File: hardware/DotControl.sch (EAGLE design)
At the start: 36 parts, among them CN1 1X4-BIG, J3 USB-MICROB, SW2 Previous, SW5 Previous, SW6 Next, SW8 Ok, U1 ATMEGA328P-MU-QFN32, U2 TMP102, U3 ATSHA204-TSU, U4 SI7021

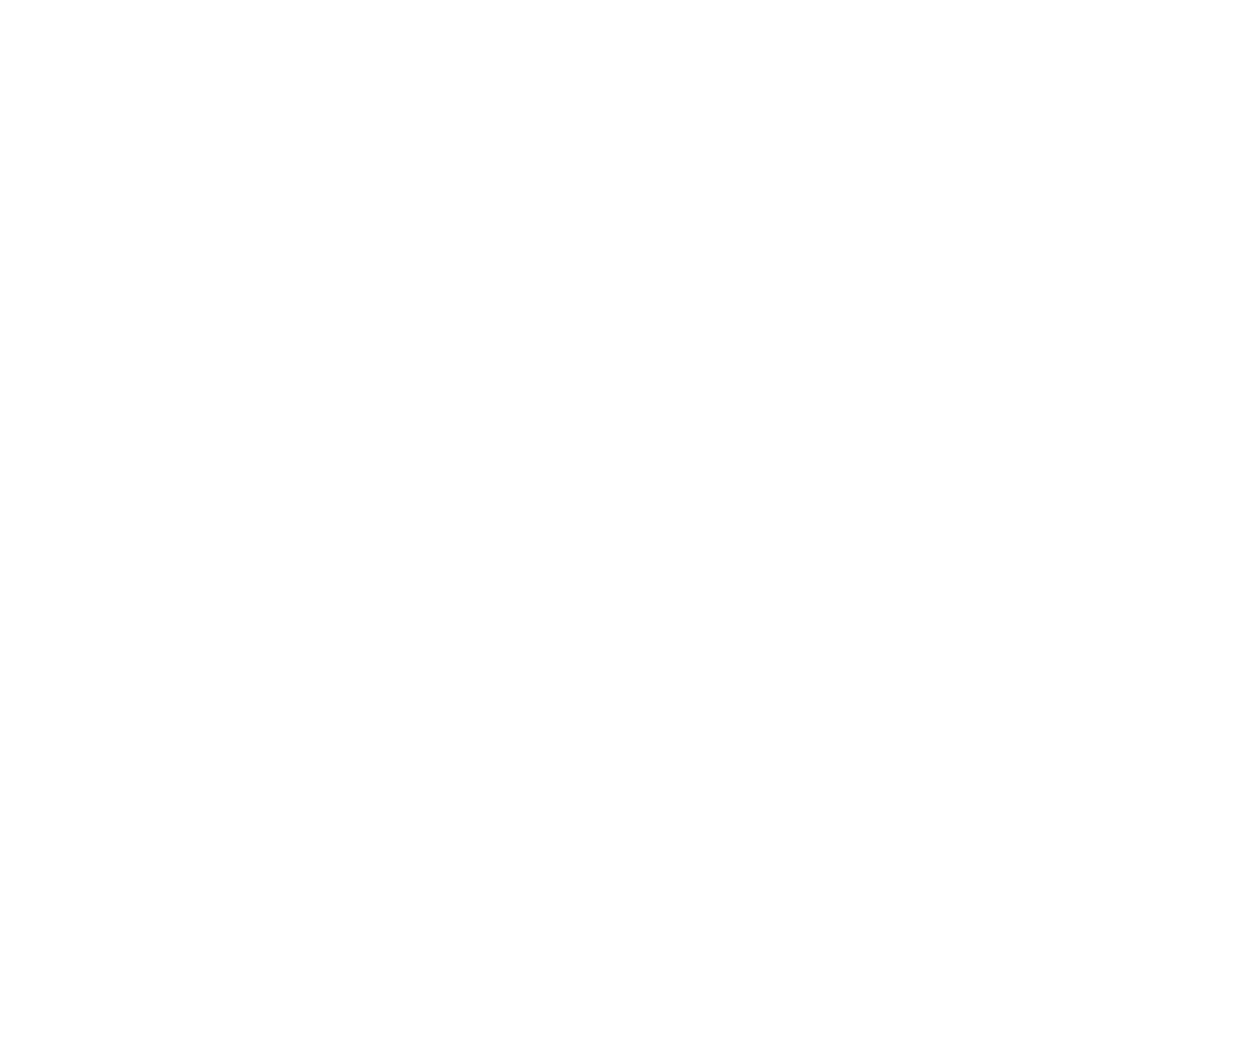
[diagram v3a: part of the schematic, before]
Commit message: [Beta] Add HW support for MPU9250
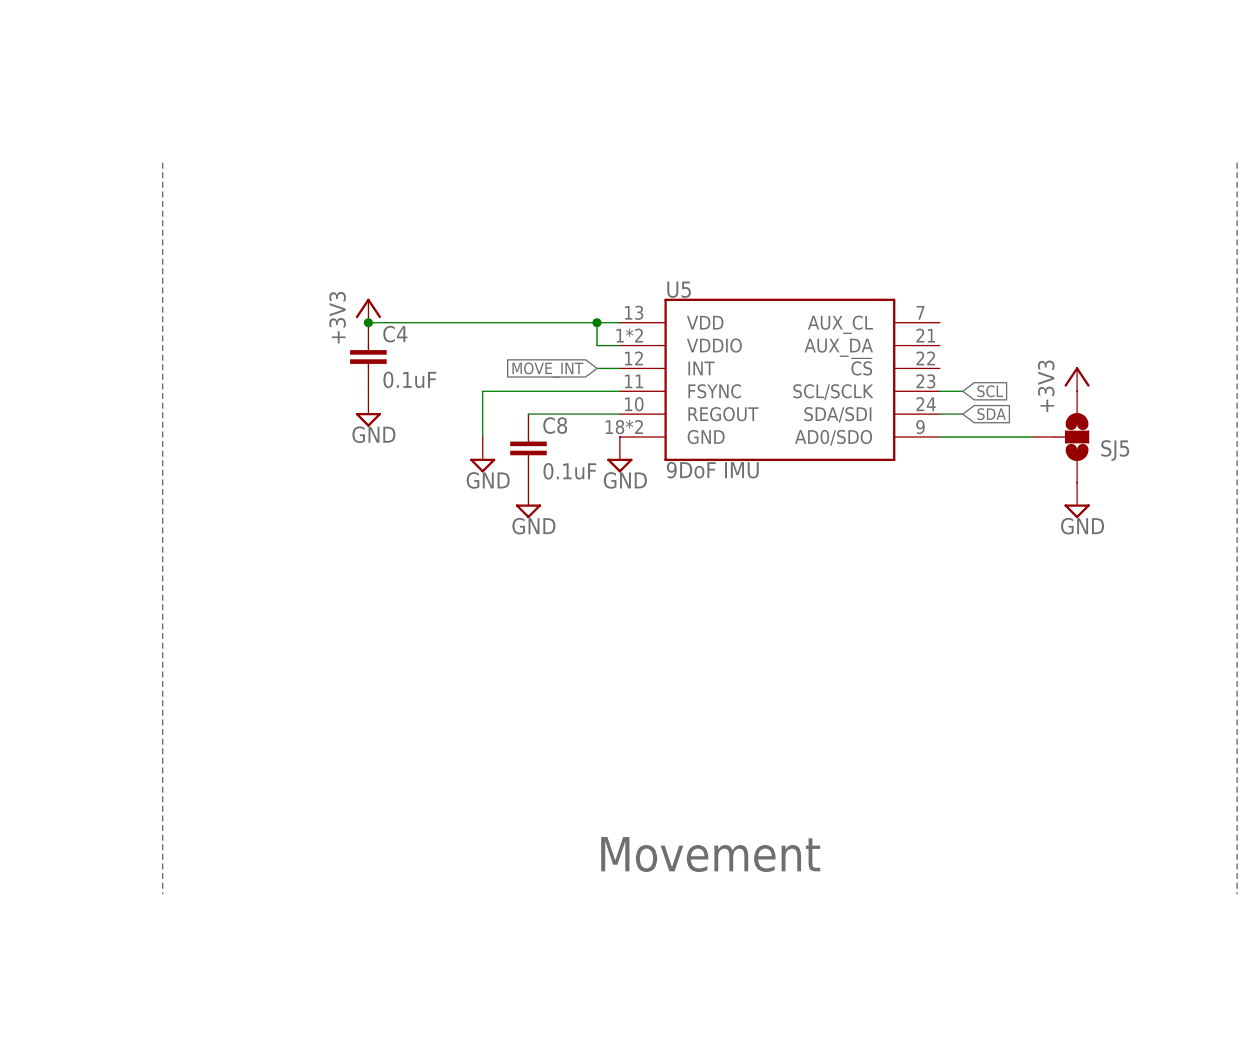
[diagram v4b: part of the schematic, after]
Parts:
- added C4, C8: 0.1uF, resistor:C-EUC0603
- added SJ5: (no value), SparkFun:SOLDERJUMPER_2WAYS
- added U5: 9DoF IMU, SparkFun-Sensors:MPU-9250
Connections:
- new net MOVE_INT: U5.INT
- new net N$10: SJ5.2, U5.AD0/SDO
- new net N$15: C8.1, U5.REGOUT
- net +3V3: now also C4.1, SJ5.3, U5.VDD, U5.VDDIO
- net GND: now also C4.2, C8.2, SJ5.1, U5.FSYNC, U5.GND
- net SCL: now also U5.SCL/SCLK
- net SDA: now also U5.SDA/SDI
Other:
- note added: "Movement"
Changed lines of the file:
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@@
 <setting verticaltext="up"/>
 </settings>
-<grid distance="0.05" unitdist="inch" unit="inch" style="lines" multiple="1" display="no" altdistance="0.01" altunitdist="inch" altunit="inch"/>
+<grid distance="0.1" unitdist="inch" unit="inch" style="lines" multiple="1" display="no" altdistance="0.01" altunitdist="inch" altunit="inch"/>
 <layers>
 <layer number="1" name="Top" color="4" fill="1" visible="no" active="no"/>
@@
 <part name="C10" library="adafruit" deviceset="CPOL-US" device="CT7343" value="1500uF 4V"/>
 <part name="SUPPLY16" library="supply2" deviceset="GND" device=""/>
+<part name="U5" library="SparkFun-Sensors" deviceset="MPU-9250" device="" value="9DoF IMU"/>
+<part name="SUPPLY23" library="supply2" deviceset="GND" device=""/>
+<part name="SJ5" library="SparkFun" deviceset="SOLDERJUMPER_2WAY" device="S"/>
+<part name="SUPPLY24" library="supply2" deviceset="GND" device=""/>
+<part name="+3V16" library="supply1" deviceset="+3V3" device=""/>
+<part name="C8" library="resistor" deviceset="C-EU" device="C0603" value="0.1uF"/>
+<part name="SUPPLY25" library="supply2" deviceset="GND" device=""/>
+<part name="+3V13" library="supply1" deviceset="+3V3" device=""/>
+<part name="C4" library="resistor" deviceset="C-EU" device="C0603" value="0.1uF"/>
+<part name="SUPPLY17" library="supply2" deviceset="GND" device=""/>
+<part name="SUPPLY28" library="supply2" deviceset="GND" device=""/>
 </parts>
 <sheets>
@@
 <text x="208.28" y="71.12" size="3.81" layer="91">Authentification module</text>
 <text x="110.49" y="96.52" size="1.27" layer="91">RGB on press</text>
+<wire x1="576.58" y1="246.38" x2="576.58" y2="165.1" width="0.1524" layer="95" style="longdash"/>
+<text x="505.46" y="167.64" size="3.81" layer="95">Movement</text>
+<wire x1="457.2" y1="246.38" x2="457.2" y2="165.1" width="0.1524" layer="95" style="longdash"/>
 </plain>
 <instances>
@@
 <instance part="C10" gate="G$1" x="134.62" y="144.78"/>
 <instance part="SUPPLY16" gate="GND" x="134.62" y="129.54"/>
+<instance part="U5" gate="G$1" x="525.78" y="220.98"/>
+<instance part="SUPPLY23" gate="GND" x="508" y="213.36"/>
+<instance part="SJ5" gate="G$1" x="558.8" y="215.9" rot="MR180"/>
+<instance part="SUPPLY24" gate="GND" x="558.8" y="208.28"/>
+<instance part="+3V16" gate="G$1" x="558.8" y="223.52"/>
+<instance part="C8" gate="G$1" x="497.84" y="215.9"/>
+<instance part="SUPPLY25" gate="GND" x="497.84" y="208.28"/>
+<instance part="+3V13" gate="G$1" x="480.06" y="231.14"/>
+<instance part="C4" gate="G$1" x="480.06" y="226.06"/>
+<instance part="SUPPLY17" gate="GND" x="480.06" y="218.44"/>
+<instance part="SUPPLY28" gate="GND" x="492.76" y="213.36"/>
 </instances>
 <busses>
@@
 <wire x1="134.62" y1="139.7" x2="134.62" y2="132.08" width="0.1524" layer="91"/>
 </segment>
+<segment>
+<pinref part="SJ5" gate="G$1" pin="1"/>
+<pinref part="SUPPLY24" gate="GND" pin="GND"/>
+</segment>
+<segment>
+<pinref part="C8" gate="G$1" pin="2"/>
+<pinref part="SUPPLY25" gate="GND" pin="GND"/>
+</segment>
+<segment>
+<pinref part="U5" gate="G$1" pin="GND"/>
+<pinref part="SUPPLY23" gate="GND" pin="GND"/>
+</segment>
+<segment>
+<pinref part="C4" gate="G$1" pin="2"/>
+<pinref part="SUPPLY17" gate="GND" pin="GND"/>
+</segment>
+<segment>
+<pinref part="U5" gate="G$1" pin="FSYNC"/>
+<wire x1="508" y1="220.98" x2="492.76" y2="220.98" width="0.1524" layer="91"/>
+<wire x1="492.76" y1="220.98" x2="492.76" y2="215.9" width="0.1524" layer="91"/>
+<pinref part="SUPPLY28" gate="GND" pin="GND"/>
+</segment>
 </net>
 <net name="SCK" class="0">
@@
 <label x="237.49" y="132.08" size="1.27" layer="95" xref="yes"/>
 </segment>
+<segment>
+<pinref part="U5" gate="G$1" pin="SDA/SDI"/>
+<wire x1="543.56" y1="218.44" x2="546.1" y2="218.44" width="0.1524" layer="91"/>
+<label x="546.1" y="218.44" size="1.27" layer="95" xref="yes"/>
+</segment>
 </net>
 <net name="SCL" class="0">
@@
 <wire x1="234.95" y1="129.54" x2="237.49" y2="129.54" width="0.1524" layer="91"/>
 <label x="237.49" y="129.54" size="1.27" layer="95" xref="yes"/>
+</segment>
+<segment>
+<pinref part="U5" gate="G$1" pin="SCL/SCLK"/>
+<wire x1="543.56" y1="220.98" x2="546.1" y2="220.98" width="0.1524" layer="91"/>
+<label x="546.1" y="220.98" size="1.27" layer="95" xref="yes"/>
 </segment>
 </net>
@@
 <wire x1="214.63" y1="137.16" x2="214.63" y2="132.08" width="0.1524" layer="91"/>
 </segment>
+<segment>
+<pinref part="SJ5" gate="G$1" pin="3"/>
+<pinref part="+3V16" gate="G$1" pin="+3V3"/>
+</segment>
+<segment>
+<pinref part="+3V13" gate="G$1" pin="+3V3"/>
+<pinref part="C4" gate="G$1" pin="1"/>
+<junction x="480.06" y="228.6"/>
+<pinref part="U5" gate="G$1" pin="VDD"/>
+<wire x1="480.06" y1="228.6" x2="505.46" y2="228.6" width="0.1524" layer="91"/>
+<pinref part="U5" gate="G$1" pin="VDDIO"/>
+<wire x1="505.46" y1="228.6" x2="508" y2="228.6" width="0.1524" layer="91"/>
+<wire x1="508" y1="226.06" x2="505.46" y2="226.06" width="0.1524" layer="91"/>
+<wire x1="505.46" y1="226.06" x2="505.46" y2="228.6" width="0.1524" layer="91"/>
+<junction x="505.46" y="228.6"/>
+</segment>
 </net>
 <net name="PUSH" class="0">
@@
 </segment>
 </net>
+<net name="MOVE_INT" class="0">
+<segment>
+<pinref part="U5" gate="G$1" pin="INT"/>
+<wire x1="508" y1="223.52" x2="505.46" y2="223.52" width="0.1524" layer="91"/>
+<label x="505.46" y="223.52" size="1.27" layer="95" rot="R180" xref="yes"/>
+</segment>
+</net>
+<net name="N$10" class="0">
+<segment>
+<pinref part="U5" gate="G$1" pin="AD0/SDO"/>
+<pinref part="SJ5" gate="G$1" pin="2"/>
+<wire x1="543.56" y1="215.9" x2="553.72" y2="215.9" width="0.1524" layer="91"/>
+</segment>
+</net>
+<net name="N$15" class="0">
+<segment>
+<pinref part="U5" gate="G$1" pin="REGOUT"/>
+<pinref part="C8" gate="G$1" pin="1"/>
+<wire x1="508" y1="218.44" x2="497.84" y2="218.44" width="0.1524" layer="91"/>
+</segment>
+</net>

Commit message: Add caps for MPU9250, V divider for battery charge
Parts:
- added C5: 100uF 4V, adafruit:C-USC3216
- added R6: 70Ω, resistor:R-EU_R0603
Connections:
- net +3V3: now also C5.1
- net GND: now also C5.2, R6.2
- net N$1: now also R6.1
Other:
- note added: "2.6V 4.289mA 2.7V 2.568mA 2.8V 1.433mA 2.9V 756uA 3V 386uA 3.1V Off"
- note added: "See Schematic Sheet 2 for further details"
- note added: "circuitlab.com simulations for battery charge Values for 10 and 70 ohm voltage divider"
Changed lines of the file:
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@@
 <part name="SUPPLY17" library="supply2" deviceset="GND" device=""/>
 <part name="SUPPLY28" library="supply2" deviceset="GND" device=""/>
+<part name="R6" library="resistor" deviceset="R-EU_" device="R0603" value="70Ω"/>
+<part name="SUPPLY20" library="supply2" deviceset="GND" device=""/>
+<part name="C5" library="adafruit" deviceset="C-US" device="C3216" value="100uF 4V"/>
+<part name="SUPPLY21" library="supply2" deviceset="GND" device=""/>
 </parts>
 <sheets>
@@
 <text x="505.46" y="167.64" size="3.81" layer="95">Movement</text>
 <wire x1="457.2" y1="246.38" x2="457.2" y2="165.1" width="0.1524" layer="95" style="longdash"/>
+<text x="116.84" y="170.18" size="1.778" layer="91">See Schematic Sheet 2 for further details</text>
 </plain>
 <instances>
@@
 <instance part="SJ1" gate="1" x="80.01" y="219.71" rot="R90"/>
 <instance part="+3V7" gate="G$1" x="80.01" y="227.33"/>
-<instance part="R1" gate="G$1" x="114.3" y="160.02" rot="R90"/>
+<instance part="R1" gate="G$1" x="114.3" y="162.56" rot="R90"/>
 <instance part="LED2" gate="G$1" x="114.3" y="152.4"/>
 <instance part="P+5" gate="1" x="114.3" y="171.45"/>
@@
 <instance part="SUPPLY17" gate="GND" x="480.06" y="218.44"/>
 <instance part="SUPPLY28" gate="GND" x="492.76" y="213.36"/>
+<instance part="R6" gate="G$1" x="104.14" y="157.48" rot="R180"/>
+<instance part="SUPPLY20" gate="GND" x="99.06" y="154.94"/>
+<instance part="C5" gate="G$1" x="160.02" y="144.78"/>
+<instance part="SUPPLY21" gate="GND" x="160.02" y="129.54"/>
 </instances>
 <busses>
@@
 <wire x1="492.76" y1="220.98" x2="492.76" y2="215.9" width="0.1524" layer="91"/>
 <pinref part="SUPPLY28" gate="GND" pin="GND"/>
+</segment>
+<segment>
+<pinref part="R6" gate="G$1" pin="2"/>
+<pinref part="SUPPLY20" gate="GND" pin="GND"/>
+</segment>
+<segment>
+<pinref part="C5" gate="G$1" pin="2"/>
+<pinref part="SUPPLY21" gate="GND" pin="GND"/>
+<wire x1="160.02" y1="139.7" x2="160.02" y2="132.08" width="0.1524" layer="91"/>
 </segment>
 </net>
@@
 <pinref part="C10" gate="G$1" pin="+"/>
 <junction x="134.62" y="147.32"/>
+<pinref part="C5" gate="G$1" pin="1"/>
+<wire x1="134.62" y1="147.32" x2="160.02" y2="147.32" width="0.1524" layer="91"/>
 </segment>
 <segment>
@@
 <segment>
 <pinref part="R1" gate="G$1" pin="2"/>
-<wire x1="114.3" y1="165.1" x2="114.3" y2="168.91" width="0.1524" layer="91"/>
+<wire x1="114.3" y1="167.64" x2="114.3" y2="168.91" width="0.1524" layer="91"/>
 <pinref part="P+5" gate="1" pin="+5V"/>
 </segment>
@@
 <pinref part="R1" gate="G$1" pin="1"/>
 <pinref part="LED2" gate="G$1" pin="A"/>
+<wire x1="114.3" y1="157.48" x2="114.3" y2="154.94" width="0.1524" layer="91"/>
+<pinref part="R6" gate="G$1" pin="1"/>
+<wire x1="109.22" y1="157.48" x2="114.3" y2="157.48" width="0.1524" layer="91"/>
+<junction x="114.3" y="157.48"/>
 </segment>
 </net>
@@
 </nets>
 </sheet>
+<sheet>
+<plain>
+<text x="2.54" y="73.66" size="1.778" layer="91">circuitlab.com simulations for battery charge
+Values for 10 and 70 ohm voltage divider</text>
+<text x="15.24" y="50.8" size="1.778" layer="91">2.6V          4.289mA
+2.7V          2.568mA
+2.8V          1.433mA
+2.9V          756uA
+3V            386uA
+3.1V         Off</text>
+</plain>
+<instances>
+</instances>
+<busses>
+</busses>
+<nets>
+</nets>
+</sheet>

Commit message: Readjust R values for charger, add Spice link
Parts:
- R1: value 10Ω -> 75Ω
- R6: value 70Ω -> 1kΩ
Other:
- note added: "Model : http://tinyurl.com/yc4ltowd"
- note removed: "2.6V 4.289mA 2.7V 2.568mA 2.8V 1.433mA 2.9V 756uA 3V 386uA 3.1V Off"
- note removed: "See Schematic Sheet 2 for further details"
- note removed: "circuitlab.com simulations for battery charge Values for 10 and 70 ohm voltage divider"
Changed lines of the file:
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@@
 <part name="SJ1" library="SparkFun" deviceset="SOLDERJUMPER" device="TRACE"/>
 <part name="+3V7" library="supply1" deviceset="+3V3" device=""/>
-<part name="R1" library="resistor" deviceset="R-EU_" device="R0603" value="10Ω"/>
+<part name="R1" library="resistor" deviceset="R-EU_" device="R0603" value="75Ω"/>
 <part name="LED2" library="SparkFun" deviceset="LED" device="0603"/>
 <part name="P+5" library="supply1" deviceset="+5V" device=""/>
@@
 <part name="SUPPLY17" library="supply2" deviceset="GND" device=""/>
 <part name="SUPPLY28" library="supply2" deviceset="GND" device=""/>
-<part name="R6" library="resistor" deviceset="R-EU_" device="R0603" value="70Ω"/>
+<part name="R6" library="resistor" deviceset="R-EU_" device="R0603" value="1kΩ"/>
 <part name="SUPPLY20" library="supply2" deviceset="GND" device=""/>
 <part name="C5" library="adafruit" deviceset="C-US" device="C3216" value="100uF 4V"/>
@@
 <text x="505.46" y="167.64" size="3.81" layer="95">Movement</text>
 <wire x1="457.2" y1="246.38" x2="457.2" y2="165.1" width="0.1524" layer="95" style="longdash"/>
-<text x="116.84" y="170.18" size="1.778" layer="91">See Schematic Sheet 2 for further details</text>
+<text x="116.84" y="167.64" size="1.778" layer="91">Model : http://tinyurl.com/yc4ltowd</text>
 </plain>
 <instances>
@@
 </nets>
 </sheet>
-<sheet>
-<plain>
-<text x="2.54" y="73.66" size="1.778" layer="91">circuitlab.com simulations for battery charge
-Values for 10 and 70 ohm voltage divider</text>
-<text x="15.24" y="50.8" size="1.778" layer="91">2.6V          4.289mA
-2.7V          2.568mA
-2.8V          1.433mA
-2.9V          756uA
-3V            386uA
-3.1V         Off</text>
-</plain>
-<instances>
-</instances>
-<busses>
-</busses>
-<nets>
-</nets>
-</sheet>

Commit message: Add pulldown on ENA pin of voltage reg to prefent 150uA quiescent current
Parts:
- added R8: >1KΩ, resistor:R-EU_R0603
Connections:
- net +5V: now also R8.2
- net GND: now also R8.1
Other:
- note added: "LeLe: * 170uA drop on LDCL015 voltage reg. Need transistor to disable it hwn only on battery. * 16Mhz crystal with 256 division still draws 630uA in MCU sleep + no display. Probably don't use crystal?"
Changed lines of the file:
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@@
 <part name="C5" library="adafruit" deviceset="C-US" device="C3216" value="100uF 4V"/>
 <part name="SUPPLY21" library="supply2" deviceset="GND" device=""/>
+<part name="R8" library="resistor" deviceset="R-EU_" device="R0603" value="&gt;1KΩ"/>
 </parts>
 <sheets>
@@
 <instance part="SUPPLY10" gate="GND" x="121.92" y="193.04"/>
 <instance part="J3" gate="G$1" x="124.46" y="203.2"/>
-<instance part="U$4" gate="G$1" x="170.18" y="200.66"/>
-<instance part="SUPPLY27" gate="GND" x="175.26" y="187.96" rot="MR0"/>
+<instance part="U$4" gate="G$1" x="170.18" y="203.2"/>
+<instance part="SUPPLY27" gate="GND" x="175.26" y="185.42" rot="MR0"/>
 <instance part="+3V19" gate="G$1" x="182.88" y="213.36"/>
 <instance part="P+4" gate="1" x="152.4" y="213.36"/>
-<instance part="C1" gate="G$1" x="187.96" y="200.66"/>
+<instance part="C1" gate="G$1" x="187.96" y="203.2"/>
 <instance part="JP3" gate="A" x="228.6" y="204.47"/>
 <instance part="+3V6" gate="G$1" x="208.28" y="201.93" rot="R90"/>
@@
 <instance part="C5" gate="G$1" x="160.02" y="144.78"/>
 <instance part="SUPPLY21" gate="GND" x="160.02" y="129.54"/>
+<instance part="R8" gate="G$1" x="160.02" y="195.58" rot="R90"/>
 </instances>
 <busses>
@@
 <pinref part="U$4" gate="G$1" pin="GND"/>
 <pinref part="SUPPLY27" gate="GND" pin="GND"/>
-<wire x1="175.26" y1="190.5" x2="175.26" y2="193.04" width="0.1524" layer="91"/>
+<wire x1="175.26" y1="187.96" x2="175.26" y2="190.5" width="0.1524" layer="91"/>
 <pinref part="C1" gate="G$1" pin="2"/>
-<wire x1="175.26" y1="193.04" x2="187.96" y2="193.04" width="0.1524" layer="91"/>
-<wire x1="187.96" y1="193.04" x2="187.96" y2="195.58" width="0.1524" layer="91"/>
-<junction x="175.26" y="193.04"/>
+<wire x1="175.26" y1="190.5" x2="175.26" y2="195.58" width="0.1524" layer="91"/>
+<wire x1="175.26" y1="195.58" x2="187.96" y2="195.58" width="0.1524" layer="91"/>
+<wire x1="187.96" y1="195.58" x2="187.96" y2="198.12" width="0.1524" layer="91"/>
+<junction x="175.26" y="195.58"/>
+<pinref part="R8" gate="G$1" pin="1"/>
+<wire x1="160.02" y1="190.5" x2="175.26" y2="190.5" width="0.1524" layer="91"/>
+<junction x="175.26" y="190.5"/>
 </segment>
 <segment>
@@
 <pinref part="U$4" gate="G$1" pin="OUT"/>
 <pinref part="+3V19" gate="G$1" pin="+3V3"/>
-<wire x1="182.88" y1="210.82" x2="182.88" y2="203.2" width="0.1524" layer="91"/>
+<wire x1="182.88" y1="210.82" x2="182.88" y2="205.74" width="0.1524" layer="91"/>
 <pinref part="C1" gate="G$1" pin="1"/>
-<wire x1="187.96" y1="203.2" x2="182.88" y2="203.2" width="0.1524" layer="91"/>
-<junction x="182.88" y="203.2"/>
+<wire x1="187.96" y1="205.74" x2="182.88" y2="205.74" width="0.1524" layer="91"/>
+<junction x="182.88" y="205.74"/>
 </segment>
 <segment>
@@
 <pinref part="P+4" gate="1" pin="+5V"/>
 <pinref part="U$4" gate="G$1" pin="VIN"/>
-<wire x1="152.4" y1="210.82" x2="152.4" y2="203.2" width="0.1524" layer="91"/>
-<wire x1="152.4" y1="203.2" x2="160.02" y2="203.2" width="0.1524" layer="91"/>
+<wire x1="152.4" y1="210.82" x2="152.4" y2="205.74" width="0.1524" layer="91"/>
+<wire x1="152.4" y1="205.74" x2="160.02" y2="205.74" width="0.1524" layer="91"/>
 <pinref part="U$4" gate="G$1" pin="ENA"/>
-<wire x1="160.02" y1="200.66" x2="160.02" y2="203.2" width="0.1524" layer="91"/>
+<wire x1="160.02" y1="203.2" x2="160.02" y2="205.74" width="0.1524" layer="91"/>
+<junction x="160.02" y="205.74"/>
+<pinref part="R8" gate="G$1" pin="2"/>
 <junction x="160.02" y="203.2"/>
+<wire x1="160.02" y1="203.2" x2="160.02" y2="200.66" width="0.1524" layer="91"/>
 </segment>
 <segment>
@@
 </nets>
 </sheet>
+<sheet>
+<plain>
+<text x="-17.78" y="86.36" size="1.778" layer="91">LeLe:
+* 170uA drop on LDCL015 voltage reg. Need transistor to disable it hwn only on battery.
+* 16Mhz crystal with 256 division still draws 630uA in MCU sleep + no display. Probably don't use crystal?</text>
+</plain>
+<instances>
+</instances>
+<busses>
+</busses>
+<nets>
+</nets>
+</sheet>
